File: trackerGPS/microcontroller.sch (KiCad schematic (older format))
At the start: 25 parts, among them IC1 PIC32MM0256GPM028-I_ML, J1 USB_A, J2 Conn, Q1 BC847BW,115, Q2 BC847BW,115, U4 REG113NA-3.3_3K, Y1 ABM8G-48.000MHZ-18-D2Y-T

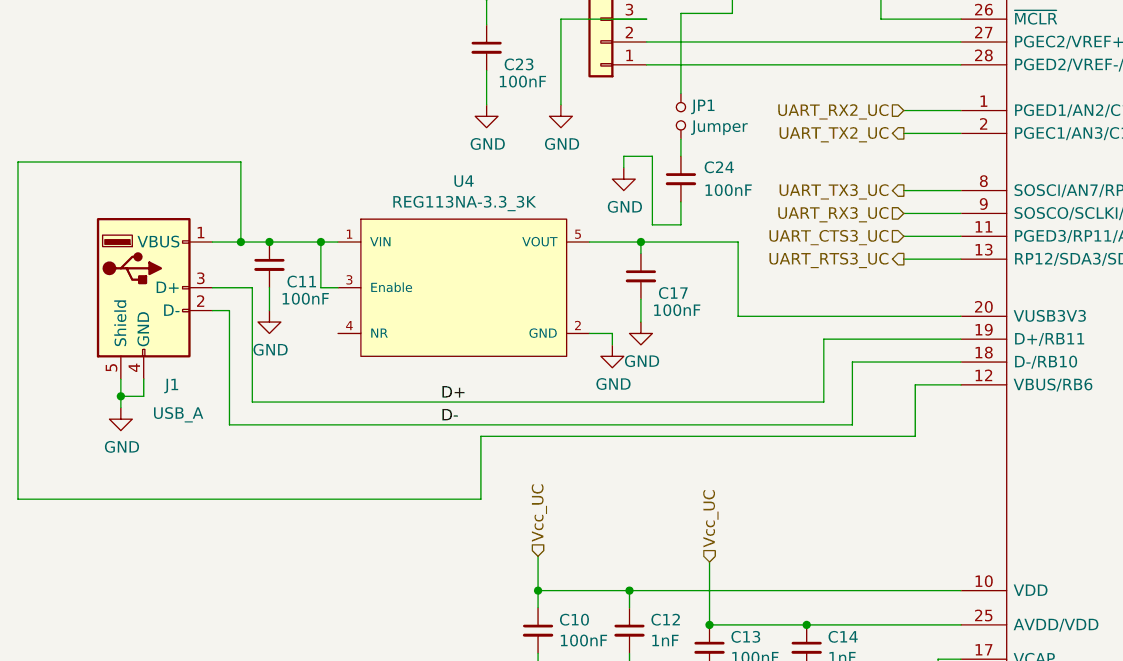
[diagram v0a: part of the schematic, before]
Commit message: Component placed 	modified:   trackerGPS/microcontroller.bak 	modified:   trackerGPS/microcontroller.sch 	modified:   trackerGPS/powerSupply.bak 	modified:   trackerGPS/powerSupply.sch 	modified:   trackerGPS/simModule.bak 	modified:   trackerGPS/simModule.sch 	modified:   trackerGPS/trackerGPS-cache.lib 	modified:   trackerGPS/trackerGPS.bak 	modified:   trackerGPS/trackerGPS.kicad_pcb 	modified:   trackerGPS/trackerGPS.kicad_pcb-bak 	modified:   trackerGPS/trackerGPS.sch
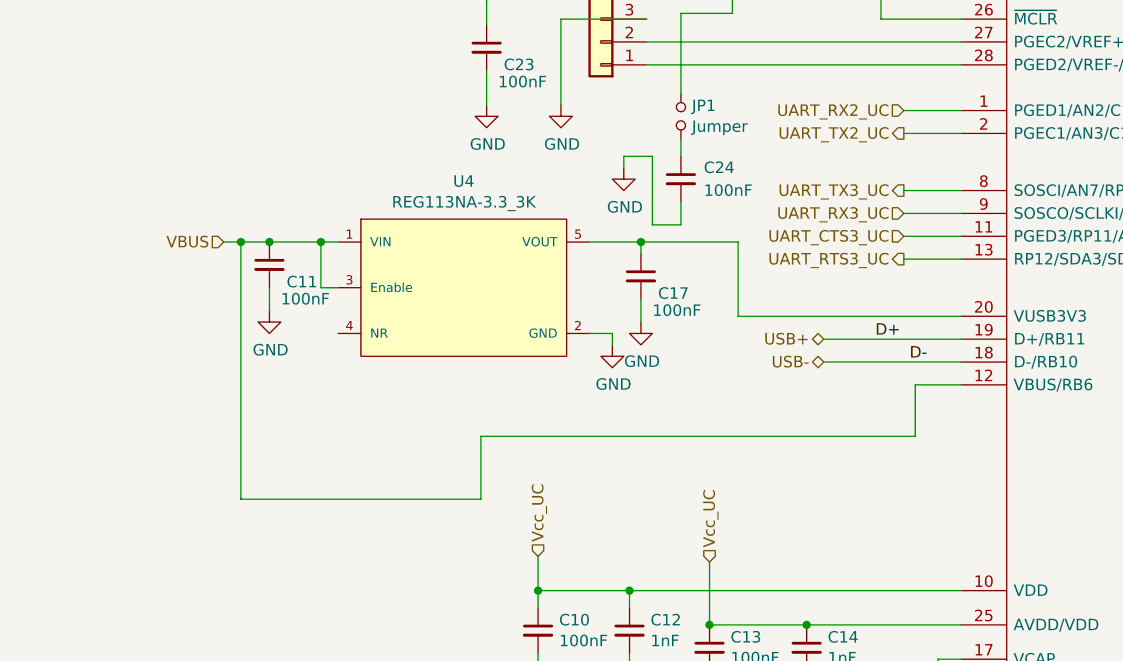
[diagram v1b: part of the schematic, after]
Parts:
- removed J1: USB_A, USB_JAE:DX4R005HJ5, symbol Connector:USB_A
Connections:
- net VBUS: now reaches C11.1, IC1.12 (VBUS/RB6), U4.1 (VIN), U4.3 (Enable)
- net D+ renamed USB+
- net D- renamed USB-
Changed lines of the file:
@@
 $Descr A3 16535 11693
 encoding utf-8
-Sheet 2 5
+Sheet 5 5
 Title ""
 Date ""
@@
 Comment4 ""
 $EndDescr
-$Comp
-L Connector:USB_A J1
-U 1 1 6058E2C5
-P 3000 4675
-F 0 "J1" H 3125 4250 50  0000 C CNN
-F 1 "USB_A" H 3150 4125 50  0000 C CNN
-F 2 "USB_JAE:DX4R005HJ5" H 3150 4625 50  0001 C CNN
-F 3 " ~" H 3150 4625 50  0001 C CNN
-	1    3000 4675
-	1    0    0    -1
-$EndComp
 Text HLabel 4725 5850 1    50   Input ~ 0
 Vcc_UC
@@
 Text HLabel 6325 4000 0    50   Output ~ 0
 UART_TX2_UC
-$Comp
-L power:GND #PWR0115
-U 1 1 605A5784
-P 2900 5200
-F 0 "#PWR0115" H 2900 4950 50  0001 C CNN
-F 1 "GND" H 2905 5027 50  0000 C CNN
-F 2 "" H 2900 5200 50  0001 C CNN
-F 3 "" H 2900 5200 50  0001 C CNN
-	1    2900 5200
-	1    0    0    -1
-$EndComp
-Wire Wire Line
-	2900 5200 2900 5150
-Wire Wire Line
-	3000 5075 3000 5150
-Wire Wire Line
-	3000 5150 2900 5150
-Connection ~ 2900 5150
-Wire Wire Line
-	2900 5150 2900 5075
 Text HLabel 6325 4550 0    50   Output ~ 0
 UART_RTS3_UC
@@
 Wire Wire Line
 	3550 4675 3550 4775
-Wire Wire Line
-	3300 4475 3425 4475
 Connection ~ 3550 4475
 $Comp
@@
 Connection ~ 5175 4475
 Wire Wire Line
-	3300 4675 3475 4675
-Wire Wire Line
-	3475 4675 3475 5175
-Wire Wire Line
-	3475 5175 5975 5175
-Wire Wire Line
-	5975 5175 5975 4900
-Wire Wire Line
 	5975 4900 6575 4900
-Wire Wire Line
-	3300 4775 3375 4775
-Wire Wire Line
-	3375 4775 3375 5275
-Wire Wire Line
-	3375 5275 6100 5275
-Wire Wire Line
-	6100 5275 6100 5000
-Wire Wire Line
-	6100 5000 6575 5000
-Text Label 4300 5175 0    50   ~ 0
+Text Label 6200 4900 0    50   ~ 0
 D+
-Text Label 4300 5275 0    50   ~ 0
+Text Label 6350 5000 0    50   ~ 0
 D-
 Text HLabel 13850 4625 2    50   Output ~ 0
@@
 	5100 4100 5100 4150
 Wire Wire Line
-	3425 4475 3425 4125
-Wire Wire Line
-	3425 4125 2450 4125
-Wire Wire Line
-	2450 4125 2450 5600
-Wire Wire Line
-	2450 5600 4475 5600
-Wire Wire Line
 	4475 5600 4475 5325
 Wire Wire Line
@@
 Wire Wire Line
 	6375 5100 6575 5100
+Wire Wire Line
+	3425 4475 3550 4475
+Wire Wire Line
+	12125 4700 12275 4700
+Wire Wire Line
+	12300 4350 12125 4350
+Wire Wire Line
+	12125 4600 12300 4600
+Text HLabel 5975 4900 0    50   BiDi ~ 0
+USB+
+Text HLabel 5975 5000 0    50   BiDi ~ 0
+USB-
+Wire Wire Line
+	5975 5000 6575 5000
+Wire Wire Line
+	3425 4475 3425 5600
+Wire Wire Line
+	3425 5600 4475 5600
+Text HLabel 3350 4475 0    50   Input ~ 0
+VBUS
+Wire Wire Line
+	3350 4475 3425 4475
 Connection ~ 3425 4475
-Wire Wire Line
-	3425 4475 3550 4475
-Wire Wire Line
-	12125 4700 12275 4700
-Wire Wire Line
-	12300 4350 12125 4350
-Wire Wire Line
-	12125 4600 12300 4600
 $EndSCHEMATC

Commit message: PCB completed with test points 	modified:   trackerGPS/gpsModule.bak 	modified:   trackerGPS/gpsModule.sch 	modified:   trackerGPS/microcontroller.bak 	modified:   trackerGPS/microcontroller.sch 	modified:   trackerGPS/powerSupply.bak 	modified:   trackerGPS/powerSupply.sch 	modified:   trackerGPS/simModule.bak 	modified:   trackerGPS/simModule.sch 	modified:   trackerGPS/trackerGPS-cache.lib 	modified:   trackerGPS/trackerGPS.bak 	modified:   trackerGPS/trackerGPS.kicad_pcb 	modified:   trackerGPS/trackerGPS.kicad_pcb-bak 	modified:   trackerGPS/trackerGPS.sch
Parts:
- removed JP1: Jumper, Connector_PinHeader_2.54mm:PinHeader_1x02_P2.54mm_Vertical, symbol Device:Jumper_NO_Small
- removed Q1: BC847BW,115, Package_TO_SOT_SMD:SOT-323_SC-70, symbol Device:Q_NPN_BEC
- removed R6: 10kOhm, Resistor_SMD:R_0805_2012Metric_Pad1.15x1.40mm_HandSolder, symbol Device:R_Small
- removed R7: 47kOhm, Resistor_SMD:R_0805_2012Metric_Pad1.15x1.40mm_HandSolder, symbol Device:R_Small
- added TP3: LDO_ENABLE, TestPoint:TestPoint_Pad_D1.0mm, symbol Connector:TestPoint
- added TP6: REF_CLK, TestPoint:TestPoint_Pad_D1.0mm, symbol Connector:TestPoint
- added TP7: VUSB3V3, TestPoint:TestPoint_Pad_D1.0mm, symbol Connector:TestPoint
- R4: value 10kOhm -> 602ohm
- R5: value 602kOhm -> 10kOhm
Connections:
- net GND: now also Y1.2 (GND_1), Y1.4 (GND_2)
- net LDO_ENABLE: now also IC1.21 (AN8/LVDIN/RP15/SCL3/SCK3/OCM3A/RB13(1)), TP3.1; no longer IC1.23 (AN10/C3INA/REFCLKO/RP17/U1RX/~SS1~/FSYNC1/OCM2B/INT0/RB15(1))
- net at C24.1: now also IC1.26 (~MCLR), R4.1, R5.1
- net VUSB3V3: now reaches C17.1, IC1.20 (VUSB3V3), U4.5 (VOUT)
- net VUSB3V3: now also TP7.1
- new net: IC1.23 (AN10/C3INA/REFCLKO/RP17/U1RX/~SS1~/FSYNC1/OCM2B/INT0/RB15(1)), TP6.1
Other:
- moved on the sheet: C24
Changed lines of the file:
@@
 	5175 4725 5175 4825
 Wire Wire Line
-	5175 4475 5600 4475
+	5175 4475 5450 4475
 Wire Wire Line
 	5600 4475 5600 4800
@@
 Text Label 6350 5000 0    50   ~ 0
 D-
-Text HLabel 13850 4625 2    50   Output ~ 0
-RESET2
-Text HLabel 12300 4600 2    50   Output ~ 0
+Text HLabel 12225 3850 2    50   Output ~ 0
 LDO_ENABLE
 Text HLabel 12275 4700 2    50   Input ~ 0
@@
 L Device:C_Small C24
 U 1 1 605BE4D1
-P 5350 4200
-F 0 "C24" H 5450 4250 50  0000 L CNN
-F 1 "100nF" H 5450 4150 50  0000 L CNN
-F 2 "Capacitor_SMD:C_0805_2012Metric_Pad1.15x1.40mm_HandSolder" H 5350 4200 50  0001 C CNN
-F 3 "~" H 5350 4200 50  0001 C CNN
-	1    5350 4200
+P 5350 3925
+F 0 "C24" H 5450 3975 50  0000 L CNN
+F 1 "100nF" H 5450 3875 50  0000 L CNN
+F 2 "Capacitor_SMD:C_0805_2012Metric_Pad1.15x1.40mm_HandSolder" H 5350 3925 50  0001 C CNN
+F 3 "~" H 5350 3925 50  0001 C CNN
+	1    5350 3925
 	1    0    0    -1
 $EndComp
@@
 	4500 3725 4500 3875
 $Comp
-L Device:Jumper_NO_Small JP1
-U 1 1 605D587B
-P 5350 3925
-F 0 "JP1" V 5396 3877 50  0000 R CNN
-F 1 "Jumper" V 5305 3877 50  0000 R CNN
-F 2 "Connector_PinHeader_2.54mm:PinHeader_1x02_P2.54mm_Vertical" H 5350 3925 50  0001 C CNN
-F 3 "~" H 5350 3925 50  0001 C CNN
-	1    5350 3925
-	0    -1   -1   0
-$EndComp
-$Comp
 L power:GND #PWR0134
 U 1 1 605D5DF8
-P 5100 4150
-F 0 "#PWR0134" H 5100 3900 50  0001 C CNN
-F 1 "GND" H 5105 3977 50  0000 C CNN
-F 2 "" H 5100 4150 50  0001 C CNN
-F 3 "" H 5100 4150 50  0001 C CNN
-	1    5100 4150
-	1    0    0    -1
-$EndComp
-Wire Wire Line
-	5350 4400 5350 4300
-Wire Wire Line
-	5350 4100 5350 4025
+P 5350 4100
+F 0 "#PWR0134" H 5350 3850 50  0001 C CNN
+F 1 "GND" H 5355 3927 50  0000 C CNN
+F 2 "" H 5350 4100 50  0001 C CNN
+F 3 "" H 5350 4100 50  0001 C CNN
+	1    5350 4100
+	1    0    0    -1
+$EndComp
 $Comp
 L power:GND #PWR0135
@@
 P 5400 3300
 F 0 "R4" V 5204 3300 50  0000 C CNN
-F 1 "10kOhm" V 5295 3300 50  0000 C CNN
+F 1 "602ohm" V 5295 3300 50  0000 C CNN
 F 2 "Resistor_SMD:R_0805_2012Metric_Pad1.15x1.40mm_HandSolder" H 5400 3300 50  0001 C CNN
 F 3 "~" H 5400 3300 50  0001 C CNN
@@
 P 5575 3075
 F 0 "R5" H 5516 3029 50  0000 R CNN
-F 1 "602kOhm" H 5516 3120 50  0000 R CNN
+F 1 "10kOhm" H 5516 3120 50  0000 R CNN
 F 2 "Resistor_SMD:R_0805_2012Metric_Pad1.15x1.40mm_HandSolder" H 5575 3075 50  0001 C CNN
 F 3 "~" H 5575 3075 50  0001 C CNN
@@
 	1    0    0    -1
 $EndComp
-$Comp
-L power:GND #PWR0136
-U 1 1 606078FE
-P 13650 5700
-F 0 "#PWR0136" H 13650 5450 50  0001 C CNN
-F 1 "GND" H 13655 5527 50  0000 C CNN
-F 2 "" H 13650 5700 50  0001 C CNN
-F 3 "" H 13650 5700 50  0001 C CNN
-	1    13650 5700
-	1    0    0    -1
-$EndComp
-$Comp
-L Device:R_Small R6
-U 1 1 60607E00
-P 12625 5250
-F 0 "R6" V 12429 5250 50  0000 C CNN
-F 1 "10kOhm" V 12520 5250 50  0000 C CNN
-F 2 "Resistor_SMD:R_0805_2012Metric_Pad1.15x1.40mm_HandSolder" H 12625 5250 50  0001 C CNN
-F 3 "~" H 12625 5250 50  0001 C CNN
-	1    12625 5250
-	0    1    1    0
-$EndComp
-Wire Wire Line
-	12125 5250 12525 5250
-Wire Wire Line
-	13650 4625 13850 4625
-Wire Wire Line
-	12725 5250 13125 5250
-$Comp
-L Device:R_Small R7
-U 1 1 6061D043
-P 13125 5500
-F 0 "R7" H 13184 5546 50  0000 L CNN
-F 1 "47kOhm" H 13184 5455 50  0000 L CNN
-F 2 "Resistor_SMD:R_0805_2012Metric_Pad1.15x1.40mm_HandSolder" H 13125 5500 50  0001 C CNN
-F 3 "~" H 13125 5500 50  0001 C CNN
-	1    13125 5500
-	1    0    0    -1
-$EndComp
-Wire Wire Line
-	13125 5400 13125 5250
-Connection ~ 13125 5250
-Wire Wire Line
-	13125 5600 13125 5650
-Wire Wire Line
-	13125 5650 13650 5650
-Connection ~ 13650 5650
-Wire Wire Line
-	13650 5650 13650 5700
-$Comp
-L Device:Q_NPN_BEC Q1
-U 1 1 60625CD6
-P 13550 5250
-F 0 "Q1" H 13741 5296 50  0000 L CNN
-F 1 "BC847BW,115" H 13741 5205 50  0000 L CNN
-F 2 "Package_TO_SOT_SMD:SOT-323_SC-70" H 13750 5350 50  0001 C CNN
-F 3 "~" H 13550 5250 50  0001 C CNN
-	1    13550 5250
-	1    0    0    -1
-$EndComp
-Wire Wire Line
-	13650 4625 13650 5050
-Wire Wire Line
-	13125 5250 13350 5250
-Wire Wire Line
-	13650 5450 13650 5650
 $Comp
 L ABM8G-12.288MHZ-18-D2Y-T:ABM8G-12.288MHZ-18-D2Y-T Y1
@@
 L power:GND #PWR0139
 U 1 1 605F11FB
-P 13025 7225
-F 0 "#PWR0139" H 13025 6975 50  0001 C CNN
-F 1 "GND" H 13030 7052 50  0000 C CNN
-F 2 "" H 13025 7225 50  0001 C CNN
-F 3 "" H 13025 7225 50  0001 C CNN
-	1    13025 7225
+P 13075 7225
+F 0 "#PWR0139" H 13075 6975 50  0001 C CNN
+F 1 "GND" H 13080 7052 50  0000 C CNN
+F 2 "" H 13075 7225 50  0001 C CNN
+F 3 "" H 13075 7225 50  0001 C CNN
+	1    13075 7225
 	1    0    0    -1
 $EndComp
@@
 L power:GND #PWR0140
 U 1 1 605F139C
-P 13175 7225
-F 0 "#PWR0140" H 13175 6975 50  0001 C CNN
-F 1 "GND" H 13180 7052 50  0000 C CNN
-F 2 "" H 13175 7225 50  0001 C CNN
-F 3 "" H 13175 7225 50  0001 C CNN
-	1    13175 7225
+P 13225 7225
+F 0 "#PWR0140" H 13225 6975 50  0001 C CNN
+F 1 "GND" H 13230 7052 50  0000 C CNN
+F 2 "" H 13225 7225 50  0001 C CNN
+F 3 "" H 13225 7225 50  0001 C CNN
+	1    13225 7225
 	1    0    0    -1
 $EndComp
@@
 Connection ~ 12675 5950
 Wire Wire Line
-	13175 7175 13175 7225
-Wire Wire Line
-	13025 7175 13025 7225
+	13225 7175 13225 7225
+Wire Wire Line
+	13075 7175 13075 7225
 $Comp
 L power:GND #PWR0145
@@
 	6325 4250 6575 4250
 Wire Wire Line
-	5350 4400 5225 4400
-Wire Wire Line
-	5225 4400 5225 4100
-Wire Wire Line
-	5225 4100 5100 4100
-Wire Wire Line
-	5100 4100 5100 4150
-Wire Wire Line
 	4475 5600 4475 5325
 Wire Wire Line
@@
 Wire Wire Line
 	12300 4350 12125 4350
-Wire Wire Line
-	12125 4600 12300 4600
 Text HLabel 5975 4900 0    50   BiDi ~ 0
 USB+
@@
 	3350 4475 3425 4475
 Connection ~ 3425 4475
+Text Label 5825 4800 0    50   ~ 0
+VUSB3V3
+Wire Wire Line
+	5350 4025 5350 4100
+$Comp
+L Connector:TestPoint TP7
+U 1 1 606DA1E1
+P 5450 5075
+F 0 "TP7" H 5392 5102 50  0000 R CNN
+F 1 "VUSB3V3" H 5392 5193 50  0000 R CNN
+F 2 "TestPoint:TestPoint_Pad_D1.0mm" H 5650 5075 50  0001 C CNN
+F 3 "~" H 5650 5075 50  0001 C CNN
+	1    5450 5075
+	-1   0    0    1
+$EndComp
+Wire Wire Line
+	5450 5075 5450 4475
+Connection ~ 5450 4475
+Wire Wire Line
+	5450 4475 5600 4475
+Wire Wire Line
+	12125 3850 12175 3850
+$Comp
+L Connector:TestPoint TP6
+U 1 1 606E0849
+P 12875 4450
+F 0 "TP6" H 12933 4570 50  0000 L CNN
+F 1 "REF_CLK" H 12933 4479 50  0000 L CNN
+F 2 "TestPoint:TestPoint_Pad_D1.0mm" H 13075 4450 50  0001 C CNN
+F 3 "~" H 13075 4450 50  0001 C CNN
+	1    12875 4450
+	1    0    0    -1
+$EndComp
+Wire Wire Line
+	12125 4600 12875 4600
+Wire Wire Line
+	12875 4600 12875 4450
+$Comp
+L Connector:TestPoint TP3
+U 1 1 606E3CC0
+P 12175 4050
+F 0 "TP3" V 12129 4238 50  0000 L CNN
+F 1 "LDO_ENABLE" V 12220 4238 50  0000 L CNN
+F 2 "TestPoint:TestPoint_Pad_D1.0mm" H 12375 4050 50  0001 C CNN
+F 3 "~" H 12375 4050 50  0001 C CNN
+	1    12175 4050
+	0    1    1    0
+$EndComp
+Wire Wire Line
+	12175 4050 12175 3850
+Connection ~ 12175 3850
+Wire Wire Line
+	12175 3850 12225 3850
 $EndSCHEMATC
